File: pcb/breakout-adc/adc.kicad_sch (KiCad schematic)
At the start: 89 parts, among them J20 Conn_02x02_Counter_Clockwise, J21 Conn_02x04_Odd_Even, U1 LMH6551MA, U2 LMH6551MA, U3 74AVC9112, U4 ADC10DL065, U5 74LS574, U6 74LS574, U7 74LS574, X1 SG-8101CE 50Mhz

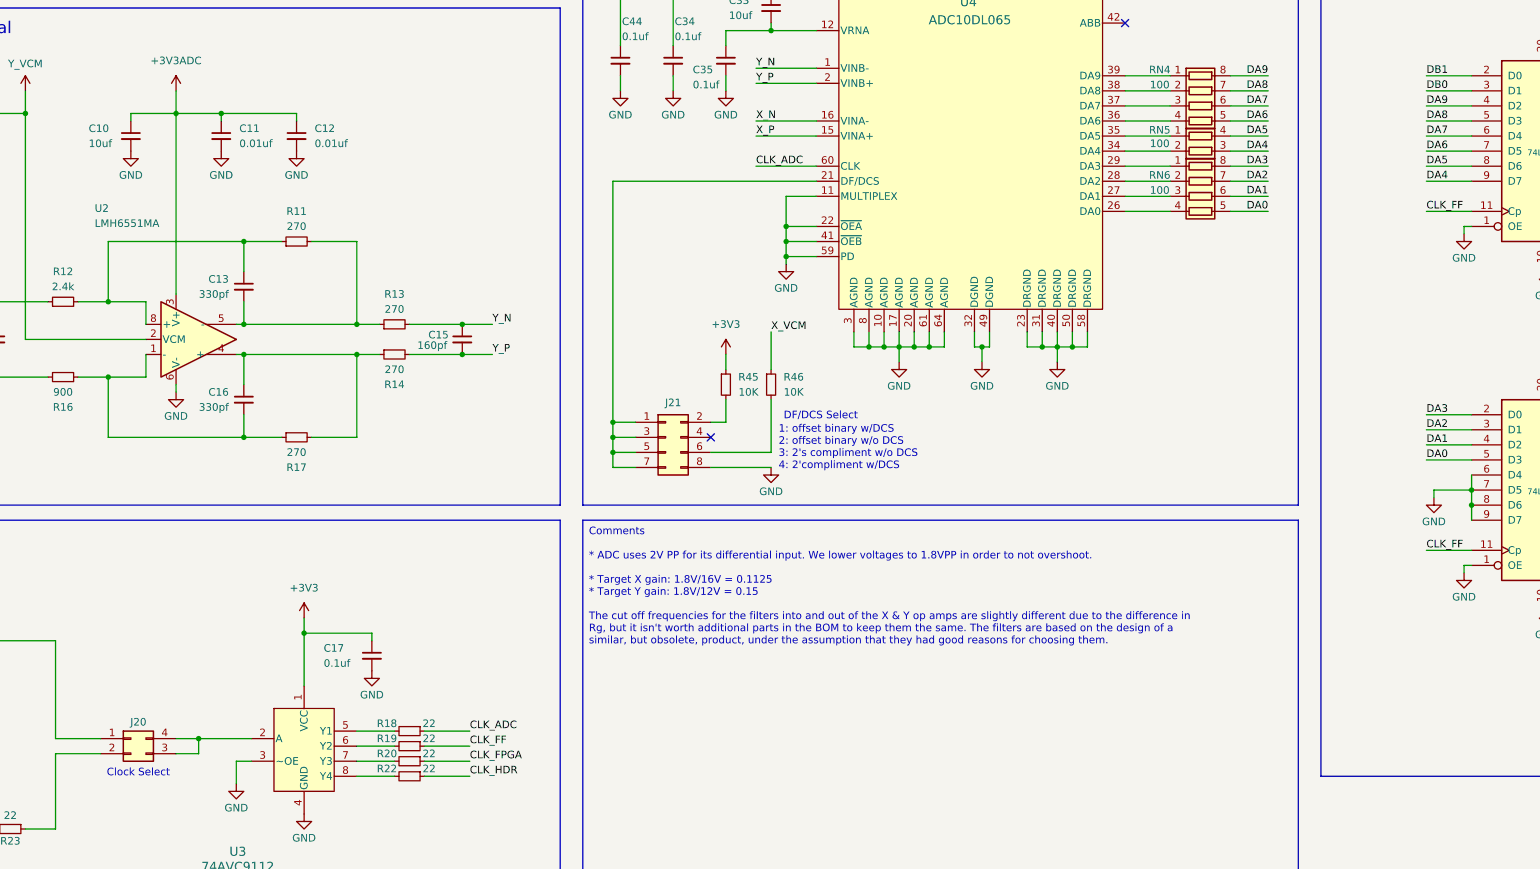
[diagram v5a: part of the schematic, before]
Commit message: [adc][pcb] redo of upper op amp
This also includes additional p&r of all components.
They are all in the pcb boundary now. This rev also
gives up on being fully single sided. See the layout.md
notes.

Lower op amp needs still needs to be placed and routed
like the upper one.
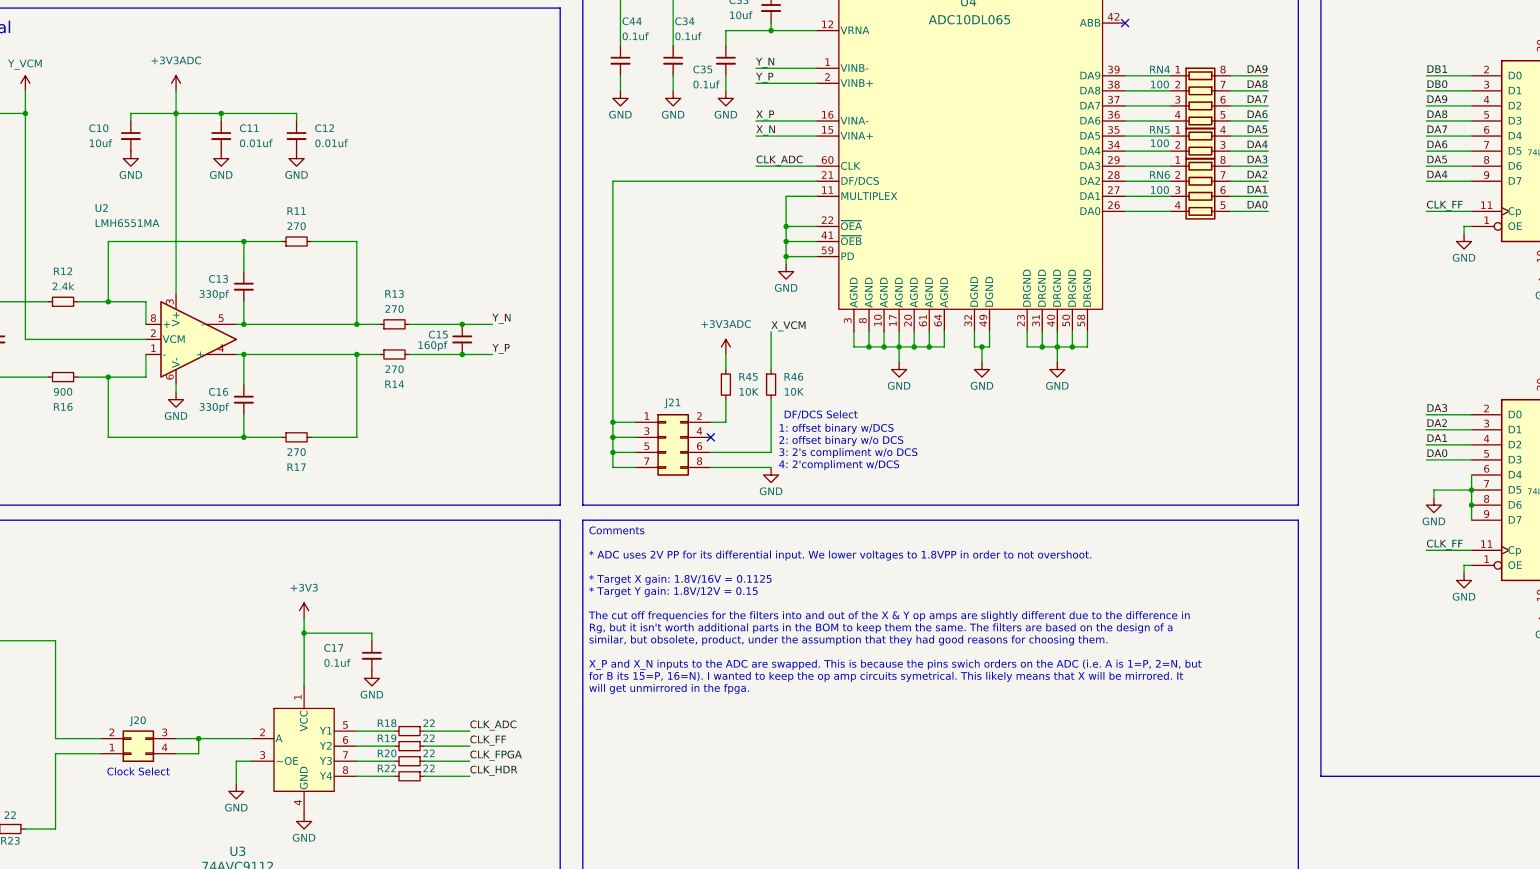
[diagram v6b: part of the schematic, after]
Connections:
- net +3V3: no longer R45.1
- net +3V3ADC: now also R45.1
- net EXT_CLK: now also J20.2 (Pin_2); no longer J20.1 (Pin_1)
- net X_N: now also U4.15 (VINA+); no longer U4.16 (VINA-)
- net X_P: now also U4.16 (VINA-); no longer U4.15 (VINA+)
- net at R23.1: now also J20.1 (Pin_1); no longer J20.2 (Pin_2)
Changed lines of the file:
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@@
 		)
 	)
-	(text_box "Comments\n\n* ADC uses 2V PP for its differential input. We lower voltages to 1.8VPP in order to not overshoot.\n\n* Target X gain: 1.8V/16V = 0.1125\n* Target Y gain: 1.8V/12V = 0.15\n\nThe cut off frequencies for the filters into and out of the X & Y op amps are slightly different due to the difference in Rg, but it isn't worth additional parts in the BOM to keep them the same. The filters are based on the design of a similar, but obsolete, product, under the assumption that they had good reasons for choosing them."
+	(text_box "Comments\n\n* ADC uses 2V PP for its differential input. We lower voltages to 1.8VPP in order to not overshoot.\n\n* Target X gain: 1.8V/16V = 0.1125\n* Target Y gain: 1.8V/12V = 0.15\n\nThe cut off frequencies for the filters into and out of the X & Y op amps are slightly different due to the difference in Rg, but it isn't worth additional parts in the BOM to keep them the same. The filters are based on the design of a similar, but obsolete, product, under the assumption that they had good reasons for choosing them.\n\nX_P and X_N inputs to the ADC are swapped. This is because the pins swich orders on the ADC (i.e. A is 1=P, 2=N, but for B its 15=P, 16=N). I wanted to keep the op amp circuits symetrical. This likely means that X will be mirrored. It will get unmirrored in the fpga."
 		(exclude_from_sim no)
 		(at 156.21 189.23 0)
@@
 	)
 	(label "X_N"
-		(at 185.42 121.92 0)
+		(at 185.42 124.46 0)
 		(fields_autoplaced yes)
 		(effects
@@
 	)
 	(label "X_P"
-		(at 185.42 124.46 0)
+		(at 185.42 121.92 0)
 		(fields_autoplaced yes)
 		(effects
@@
 	)
 	(symbol
-		(lib_id "power:+3V3")
-		(at 180.34 161.29 0)
-		(mirror y)
-		(unit 1)
-		(exclude_from_sim no)
-		(in_bom yes)
-		(on_board yes)
-		(dnp no)
-		(property "Reference" "#PWR010"
-			(at 180.34 165.1 0)
-			(effects
-				(font
-					(size 1.27 1.27)
-				)
-				(hide yes)
-			)
-		)
-		(property "Value" "+3V3"
-			(at 180.34 156.21 0)
-			(effects
-				(font
-					(size 1.27 1.27)
-				)
-			)
-		)
-		(property "Footprint" ""
-			(at 180.34 161.29 0)
-			(effects
-				(font
-					(size 1.27 1.27)
-				)
-				(hide yes)
-			)
-		)
-		(property "Datasheet" ""
-			(at 180.34 161.29 0)
-			(effects
-				(font
-					(size 1.27 1.27)
-				)
-				(hide yes)
-			)
-		)
-		(property "Description" "Power symbol creates a global label with name \"+3V3\""
-			(at 180.34 161.29 0)
-			(effects
-				(font
-					(size 1.27 1.27)
-				)
-				(hide yes)
-			)
-		)
-		(pin "1"
-		)
-		(instances
-			(project "breakout-adc"
-				(path "/912c7b42-54cd-43e2-8ab1-2cdab401e0a2/72f7b3b0-9aad-456f-b2b7-645b743c86eb"
-					(reference "#PWR010")
-					(unit 1)
-				)
-			)
-		)
-	)
-	(symbol
 		(lib_id "Device:R_Pack04")
 		(at 260.35 134.62 270)
@@
 	(symbol
 		(lib_id "Connector_Generic:Conn_02x02_Counter_Clockwise")
-		(at 80.01 226.06 0)
+		(at 80.01 228.6 0)
+		(mirror x)
 		(unit 1)
 		(exclude_from_sim yes)
@@
 		(dnp no)
 		(property "Reference" "J20"
-			(at 81.28 223.266 0)
+			(at 81.28 223.012 0)
 			(effects
 				(font
@@
 		)
 		(property "Value" "Conn_02x02_Counter_Clockwise"
-			(at 81.28 222.25 0)
+			(at 81.28 232.41 0)
 			(effects
 				(font
@@
 		)
 		(property "Footprint" "Connector_PinHeader_2.54mm:PinHeader_2x02_P2.54mm_Vertical"
-			(at 80.01 226.06 0)
+			(at 80.01 228.6 0)
 			(effects
 				(font
@@
 		)
 		(property "Datasheet" "~"
-			(at 80.01 226.06 0)
+			(at 80.01 228.6 0)
 			(effects
 				(font
@@
 		)
 		(property "Description" "Generic connector, double row, 02x02, counter clockwise pin numbering scheme (similar to DIP package numbering), script generated (kicad-library-utils/schlib/autogen/connector/)"
-			(at 80.01 226.06 0)
+			(at 80.01 228.6 0)
 			(effects
 				(font
@@
 					(unit 1)
 				)
+			)
+		)
+	)
+	(symbol
+		(lib_id "power:+3.3VA")
+		(at 180.34 161.29 0)
+		(unit 1)
+		(exclude_from_sim no)
+		(in_bom yes)
+		(on_board yes)
+		(dnp no)
+		(fields_autoplaced yes)
+		(property "Reference" "#PWR010"
+			(at 180.34 165.1 0)
+			(effects
+				(font
+					(size 1.27 1.27)
+				)
+				(hide yes)
+			)
+		)
+		(property "Value" "+3V3ADC"
+			(at 180.34 156.21 0)
+			(effects
+				(font
+					(size 1.27 1.27)
+				)
+			)
+		)
+		(property "Footprint" ""
+			(at 180.34 161.29 0)
+			(effects
+				(font
+					(size 1.27 1.27)
+				)
+				(hide yes)
+			)
+		)
+		(property "Datasheet" ""
+			(at 180.34 161.29 0)
+			(effects
+				(font
+					(size 1.27 1.27)
+				)
+				(hide yes)
+			)
+		)
+		(property "Description" "Power symbol creates a global label with name \"+3.3VA\""
+			(at 180.34 161.29 0)
+			(effects
+				(font
+					(size 1.27 1.27)
+				)
+				(hide yes)
+			)
+		)
+		(pin "1"
+		)
+		(instances
+			(project "breakout-adc"
+				(path "/912c7b42-54cd-43e2-8ab1-2cdab401e0a2/72f7b3b0-9aad-456f-b2b7-645b743c86eb"
+					(reference "#PWR010")
+					(unit 1)
+				)

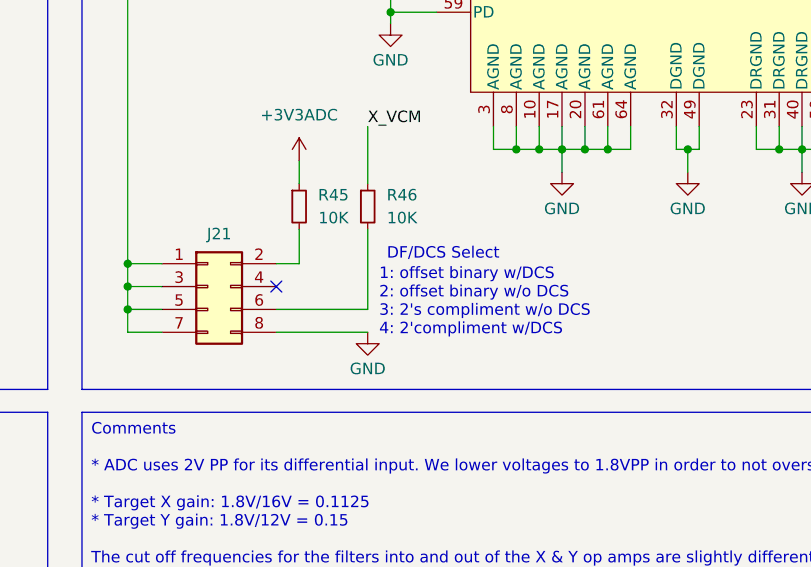
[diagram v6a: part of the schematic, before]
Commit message: [adc][pcb] adc jumper select silks
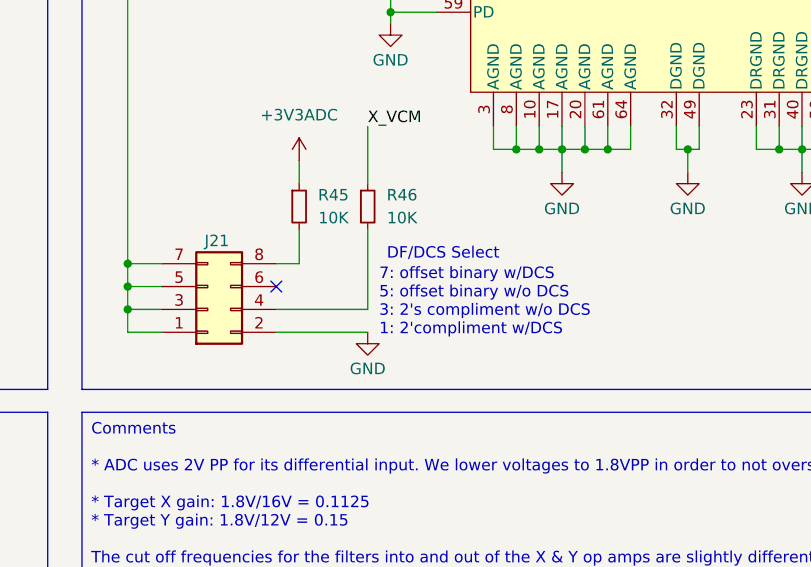
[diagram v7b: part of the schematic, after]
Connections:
- net GND: now also J21.2 (Pin_2); no longer J21.8 (Pin_8)
- net at R46.2: now also J21.4 (Pin_4); no longer J21.6 (Pin_6)
- net at R45.2: now also J21.8 (Pin_8); no longer J21.2 (Pin_2)
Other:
- note added: "7: offset binary w/DCS 5: offset binary w/o DCS 3: 2's compliment w/o DCS 1: 2'compliment w/DCS"
- note removed: "1: offset binary w/DCS 2: offset binary w/o DCS 3: 2's compliment w/o DCS 4: 2'compliment w/DCS"
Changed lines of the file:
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@@
 		)
 	)
-	(text "1: offset binary w/DCS\n2: offset binary w/o DCS\n3: 2's compliment w/o DCS\n4: 2'compliment w/DCS"
+	(text "7: offset binary w/DCS\n5: offset binary w/o DCS\n3: 2's compliment w/o DCS\n1: 2'compliment w/DCS"
 		(exclude_from_sim no)
 		(at 189.23 177.038 0)
@@
 	(symbol
 		(lib_id "Connector_Generic:Conn_02x04_Odd_Even")
-		(at 170.18 175.26 0)
+		(at 170.18 177.8 0)
+		(mirror x)
 		(unit 1)
 		(exclude_from_sim yes)
@@
 		(dnp no)
 		(property "Reference" "J21"
-			(at 171.45 169.418 0)
+			(at 171.196 170.18 0)
 			(effects
 				(font
@@
 		)
 		(property "Value" "Conn_02x04_Odd_Even"
-			(at 171.45 168.91 0)
+			(at 171.45 184.15 0)
 			(effects
 				(font
@@
 		)
 		(property "Footprint" "Connector_PinHeader_2.54mm:PinHeader_2x04_P2.54mm_Vertical"
-			(at 170.18 175.26 0)
+			(at 170.18 177.8 0)
 			(effects
 				(font
@@
 		)
 		(property "Datasheet" "~"
-			(at 170.18 175.26 0)
+			(at 170.18 177.8 0)
 			(effects
 				(font
@@
 		)
 		(property "Description" "Generic connector, double row, 02x04, odd/even pin numbering scheme (row 1 odd numbers, row 2 even numbers), script generated (kicad-library-utils/schlib/autogen/connector/)"
-			(at 170.18 175.26 0)
+			(at 170.18 177.8 0)
 			(effects
 				(font

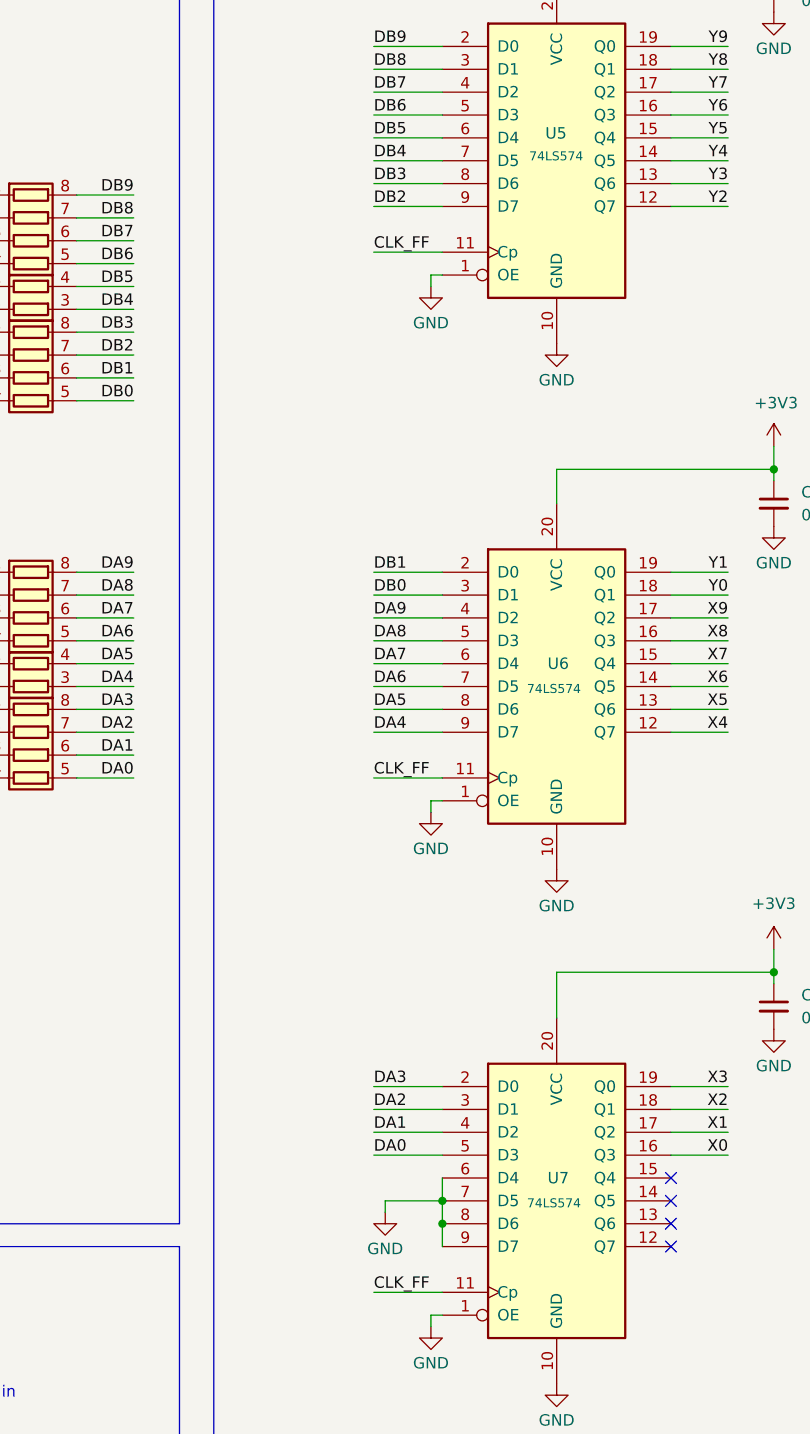
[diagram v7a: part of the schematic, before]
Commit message: [adc][pcb] flip flop inputs routed
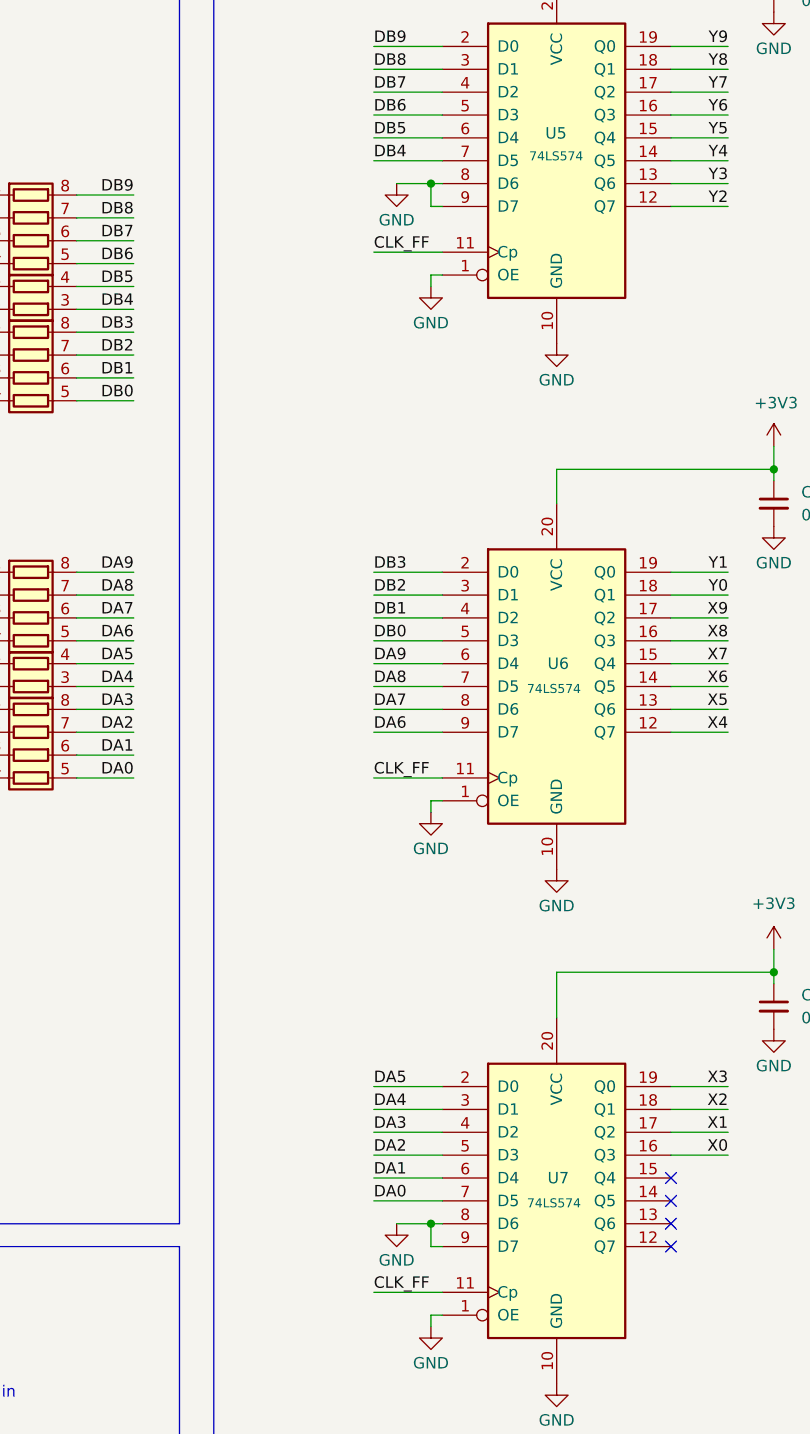
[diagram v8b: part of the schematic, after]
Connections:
- net DA0: now also U7.7 (D5); no longer U7.5 (D3)
- net DA1: now also U7.6 (D4); no longer U7.4 (D2)
- net DA2: now also U7.5 (D3); no longer U7.3 (D1)
- net DA3: now also U7.4 (D2); no longer U7.2 (D0)
- net DA4: now also U7.3 (D1); no longer U6.9 (D7)
- net DA5: now also U7.2 (D0); no longer U6.8 (D6)
- net DA6: now also U6.9 (D7); no longer U6.7 (D5)
- net DA7: now also U6.8 (D6); no longer U6.6 (D4)
- net DA8: now also U6.7 (D5); no longer U6.5 (D3)
- net DA9: now also U6.6 (D4); no longer U6.4 (D2)
- net DB0: now also U6.5 (D3); no longer U6.3 (D1)
- net DB1: now also U6.4 (D2); no longer U6.2 (D0)
- net DB2: now also U6.3 (D1); no longer U5.9 (D7)
- net DB3: now also U6.2 (D0); no longer U5.8 (D6)
- net GND: now also U5.8 (D6), U5.9 (D7); no longer U7.6 (D4), U7.7 (D5)
